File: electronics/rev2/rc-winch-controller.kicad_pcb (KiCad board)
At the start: 2 copper layers, 30 x 16 mm, 13 parts, among them J1 Conn_01x06, J2 Conn_01x06, SW1 SETUP, U1 MCP1703A-3302_SOT23, U2 LPC812M001JDH16, U3 RZ7889

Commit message: Update layout and silkscreen
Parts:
- F1: value 3A 16V 1812 -> 4A 16V 1812
- moved RN1 0.41 mm to (123.9, 91.8)
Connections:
- RN1 pad 3: /AUX-Rx-in -> /Tx-in
- RN1 pad 4: /Tx-in -> /AUX-Rx-in
- RN1 pad 5: /Tx -> /AUX-Rx
- RN1 pad 6: /AUX-Rx -> /Tx
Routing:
- net /Tx-in: track 3.52 -> 6.82 mm
- net /Tx: track 11.1 -> 9.23 mm
- net /LED-A: track 7.77 -> 6.45 mm
- net /VDD: track 23.5 -> 24.7 mm
- net /AUX-Rx: track 18.4 -> 19.6 mm
- net /AUX-Rx-in: track 4.66 -> 5.39 mm
- net GND: vias 8 -> 7
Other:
- board text added: "Winch+"
- board text removed: "+Motor"

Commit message: Tweak placement, layout and silk screen
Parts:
- moved F1 3.43 mm to (107.5, 87.0), turned to 0 degrees
- moved U3 0.64 mm to (108.3, 96.2)
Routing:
- net /VDD: track 24.7 -> 22.9 mm
- net GND: track 16.9 -> 17.8 mm, vias 7 -> 8
- net /VMOT-in: track 4.69 -> 4.12 mm

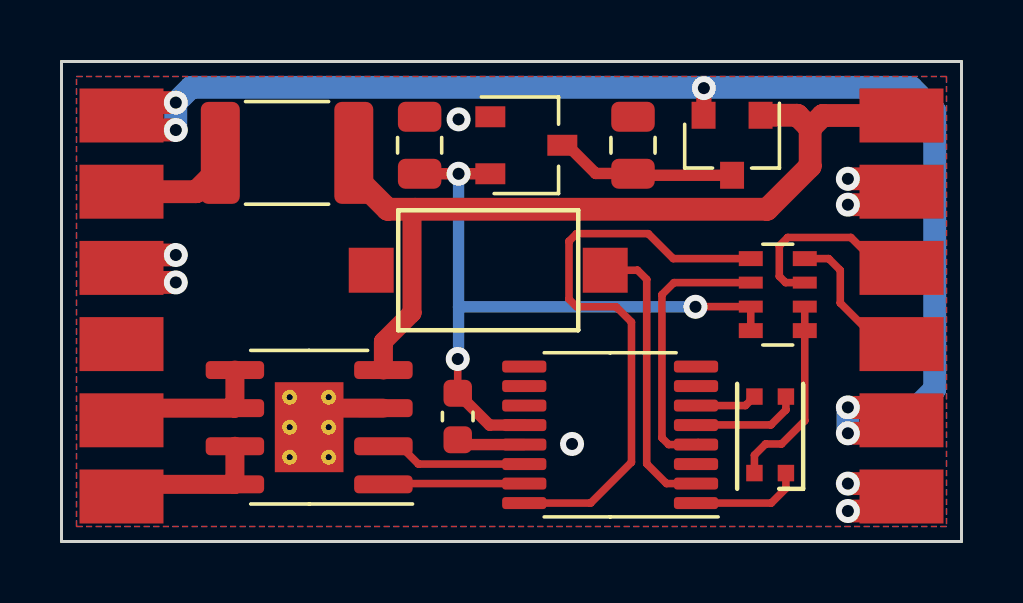
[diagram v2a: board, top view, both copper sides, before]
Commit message: Change MCU to TSSOP 20 version
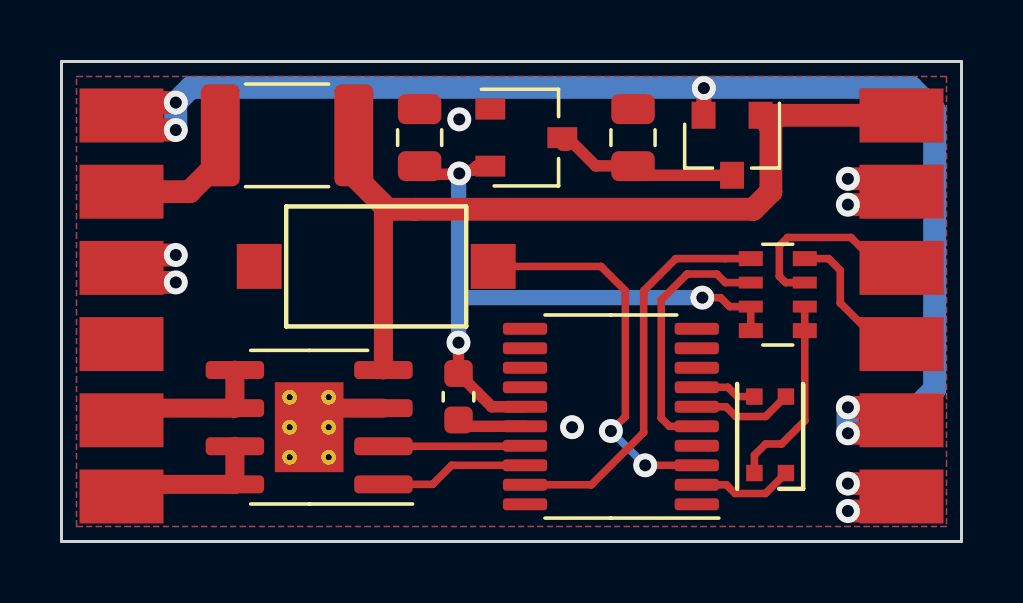
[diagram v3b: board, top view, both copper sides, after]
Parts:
- D1: value D_Schottky_x2_KCom_AAK -> BAT54C
- U1: value MCP1703A-3302_SOT23 -> ME6209A33M3G
- U2: value LPC812M001JDH16 -> LPC812M101JDH20; footprint Package_SO:TSSOP-16_4.4x5mm_P0.65mm -> Package_SO:TSSOP-20_4.4x6.5mm_P0.65mm
- moved SW1 3.74 mm to (110.5, 90.8)
- moved C3 0.66 mm to (113.2, 95.2)
- moved U2 0.61 mm to (118.3, 95.8)
- moved F1 0.58 mm to (107.5, 86.5)
- moved C1 0.25 mm to (119.0, 86.5)
- moved C2 0.25 mm to (111.9, 86.5)
- moved U1 0.25 mm to (115.5, 86.5)
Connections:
- C2 pad 1: /VDD -> +3V3
- C3 pad 1: /VDD -> +3V3
- RN1 pad 7: /VDD -> +3V3
- RN1 pad 8: /VDD -> +3V3
- U1 pad 2: /VDD -> +3V3
- U2 pad 1: /LED-R -> (no net)
- U2 pad 12: /VDD -> (no net)
- U2 pad 13: GND -> (no net)
- U2 pad 14: /REV -> (no net)
- U2 pad 15: /FWD -> +3V3
- U2 pad 16: /AUX-Rx -> GND
- U2 pad 2: /SW-ISP -> /LED-R
- U2 pad 3: (no net) -> /SW-ISP
- U2 pad 4: /Tx -> (no net)
- U2 pad 5: /LED-G -> /Tx
- U2 pad 6: /LED-B -> /LED-G
- U2 pad 7: (no net) -> /LED-B
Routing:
- net /VDD: track 22.9 -> 0.00 mm, vias 3 -> 0
- net +3V3: track 0.00 -> 22.6 mm, vias 0 -> 3
- net /AUX-Rx: track 19.6 -> 13.4 mm
- net /SW-ISP: track 9.57 -> 13.0 mm, vias 0 -> 2
- net /Tx: track 9.23 -> 8.71 mm
- net /VMOT: track 29.8 -> 30.3 mm

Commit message: Fix LED footprint and current limiting resistor
1k is enough for red and green.
It is a bit dark for blue, but 500R is too bright
for red and green.
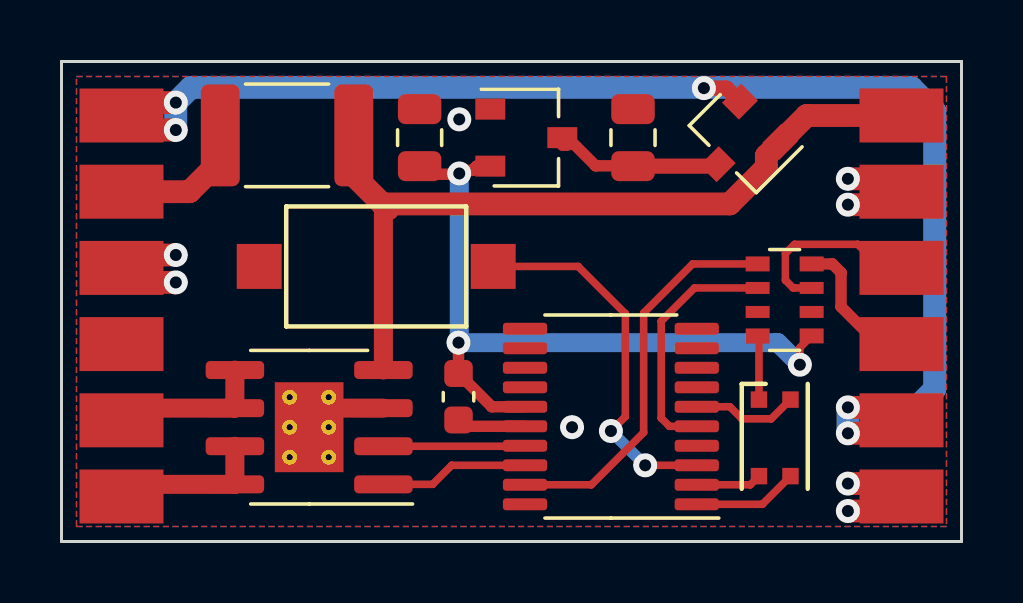
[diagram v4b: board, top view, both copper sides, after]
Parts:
- moved RN1 0.29 mm to (124.1, 91.9)
- moved D1 0.24 mm to (122.6, 86.7), turned to 225 degrees
- moved D2 0.18 mm to (123.8, 96.5), turned to 270 degrees
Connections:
- RN1 pad 1: /LED-A -> +3V3
- RN1 pad 2: /LED-A -> (no net)
- RN1 pad 7: +3V3 -> (no net)
- RN1 pad 8: +3V3 -> /LED-A
- U2 pad 1: (no net) -> /LED-G
- U2 pad 2: /LED-R -> /LED-B
- U2 pad 6: /LED-G -> /LED-R
- U2 pad 7: /LED-B -> (no net)
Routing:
- net /LED-A: track 6.56 -> 2.14 mm
- net /VMOT: track 30.3 -> 27.9 mm
- net +3V3: track 22.6 -> 24.8 mm

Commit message: Improve layout
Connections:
- RN1 pad 1: +3V3 -> /LED-A
- RN1 pad 7: (no net) -> +3V3
- RN1 pad 8: /LED-A -> +3V3
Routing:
- net /LED-A: track 2.14 -> 3.19 mm
- net +3V3: track 24.8 -> 24.0 mm
